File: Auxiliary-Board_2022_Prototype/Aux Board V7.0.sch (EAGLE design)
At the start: 56 parts, among them CON11 1X01, CON12 1X01, CON13 1X01, CON14 1X01, CON15 1X01, CON16 1X01, CON17 1X01, CON18 1X01, CON5 1X01, CON8 1X01, IC1 RS232-TTL_MAX232E

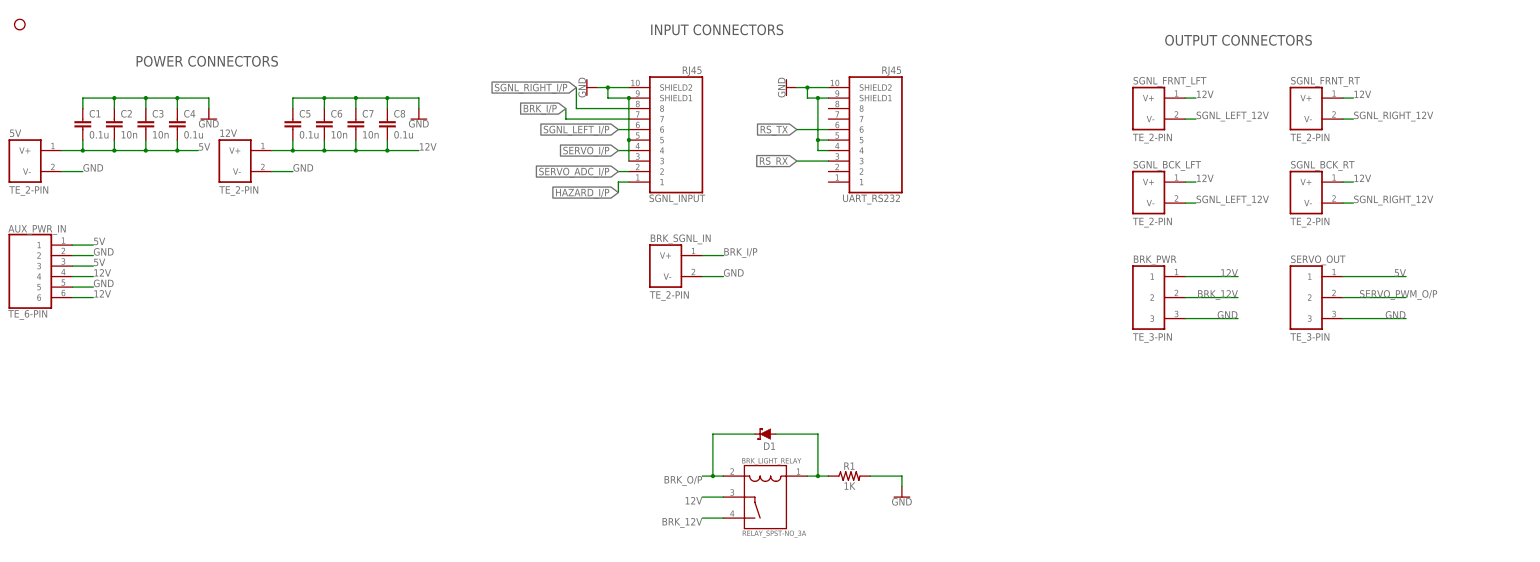
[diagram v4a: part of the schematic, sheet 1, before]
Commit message: feat: add EcoCar logo and version on board
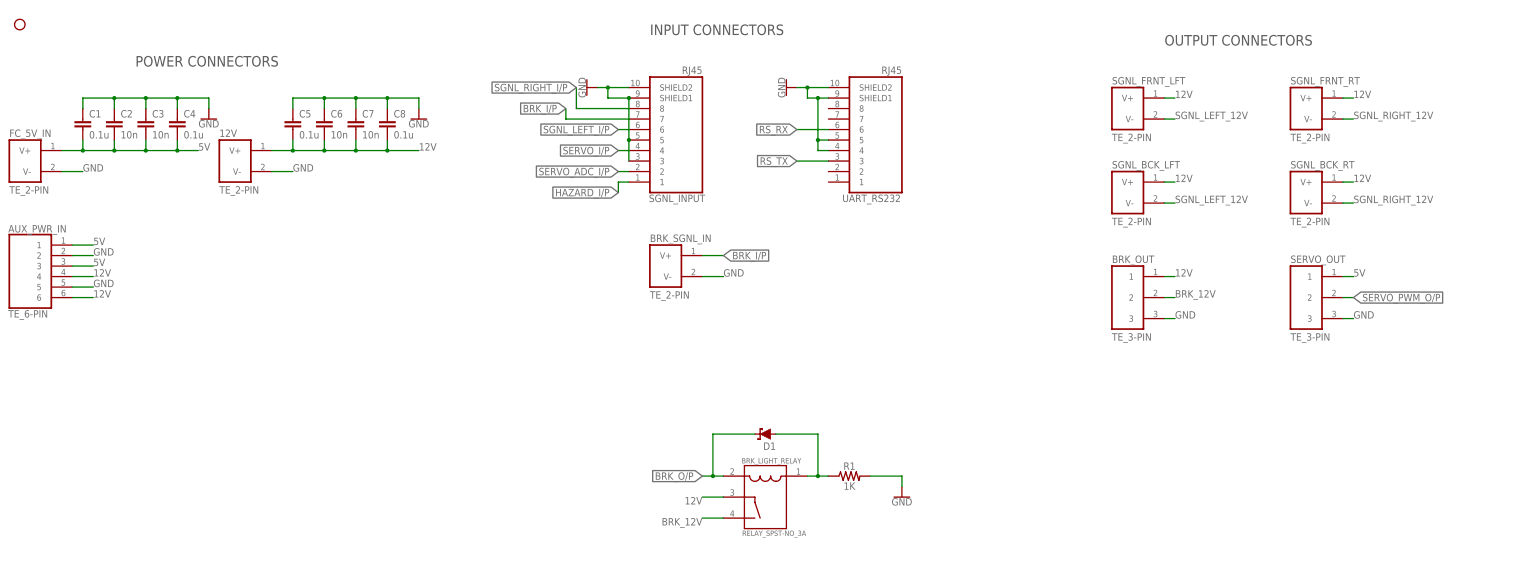
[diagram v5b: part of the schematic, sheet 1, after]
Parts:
- removed BRK_PWR: TE_3-PIN, EcoCar-Connectors:TE_3-PIN
- added BRK_OUT: TE_3-PIN, EcoCar-Connectors:TE_3-PIN
- renumbered 5V to FC_5V_IN
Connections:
- net 12V: now also BRK_OUT.1; no longer BRK_PWR.1
- net BRK_12V: now also BRK_OUT.2; no longer BRK_PWR.2
- net GND: now also BRK_OUT.3; no longer BRK_PWR.3
- net RS_RX: now also UART_RS232.6; no longer UART_RS232.3
- net RS_TX: now also UART_RS232.3; no longer UART_RS232.6
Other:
- moved on the sheet: SGNL_BCK_LFT, SGNL_FRNT_LFT
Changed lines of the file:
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@@
 <part name="CON17" library="EcoCar-Connectors-2.54mm" deviceset="1X01" device=""/>
 <part name="CON18" library="EcoCar-Connectors-2.54mm" deviceset="1X01" device=""/>
-<part name="5V" library="EcoCar-Connectors" deviceset="TE_2-PIN" device=""/>
+<part name="FC_5V_IN" library="EcoCar-Connectors" deviceset="TE_2-PIN" device=""/>
 <part name="12V" library="EcoCar-Connectors" deviceset="TE_2-PIN" device=""/>
-<part name="BRK_PWR" library="EcoCar-Connectors" deviceset="TE_3-PIN" device=""/>
+<part name="BRK_OUT" library="EcoCar-Connectors" deviceset="TE_3-PIN" device=""/>
 <part name="SERVO_OUT" library="EcoCar-Connectors" deviceset="TE_3-PIN" device=""/>
 <part name="C2" library="EcoCar-Passives" deviceset="CAPACITOR_0805" device="" value="10n"/>
@@
 <attribute name="NAME" x="274.32" y="-42.672" size="1.778" layer="95" font="vector"/>
 </instance>
-<instance part="5V" gate="G$1" x="-76.2" y="106.68" smashed="yes">
+<instance part="FC_5V_IN" gate="G$1" x="-76.2" y="106.68" smashed="yes">
 <attribute name="NAME" x="-76.2" y="117.602" size="1.778" layer="95" font="vector"/>
 <attribute name="VALUE" x="-76.2" y="103.886" size="1.778" layer="96" font="vector"/>
@@
 <attribute name="VALUE" x="-25.4" y="103.886" size="1.778" layer="96" font="vector"/>
 </instance>
-<instance part="BRK_PWR" gate="G$1" x="195.58" y="71.12" smashed="yes">
-<attribute name="NAME" x="195.58" y="87.122" size="1.778" layer="95" font="vector"/>
-<attribute name="VALUE" x="195.58" y="68.326" size="1.778" layer="96" font="vector"/>
+<instance part="BRK_OUT" gate="G$1" x="190.5" y="71.12" smashed="yes">
+<attribute name="NAME" x="190.5" y="87.122" size="1.778" layer="95" font="vector"/>
+<attribute name="VALUE" x="190.5" y="68.326" size="1.778" layer="96" font="vector"/>
 </instance>
 <instance part="SERVO_OUT" gate="G$1" x="233.68" y="71.12" smashed="yes">
@@
 <attribute name="VALUE" x="-76.454" y="73.914" size="1.778" layer="96" font="vector"/>
 </instance>
-<instance part="SGNL_FRNT_LFT" gate="G$1" x="195.58" y="119.38" smashed="yes">
-<attribute name="NAME" x="195.58" y="130.302" size="1.778" layer="95" font="vector"/>
-<attribute name="VALUE" x="195.58" y="116.586" size="1.778" layer="96" font="vector"/>
+<instance part="SGNL_FRNT_LFT" gate="G$1" x="190.5" y="119.38" smashed="yes">
+<attribute name="NAME" x="190.5" y="130.302" size="1.778" layer="95" font="vector"/>
+<attribute name="VALUE" x="190.5" y="116.586" size="1.778" layer="96" font="vector"/>
 </instance>
 <instance part="SGNL_FRNT_RT" gate="G$1" x="233.68" y="119.38" smashed="yes">
@@
 <attribute name="VALUE" x="233.68" y="116.586" size="1.778" layer="96" font="vector"/>
 </instance>
-<instance part="SGNL_BCK_LFT" gate="G$1" x="195.58" y="99.06" smashed="yes">
-<attribute name="NAME" x="195.58" y="109.982" size="1.778" layer="95" font="vector"/>
-<attribute name="VALUE" x="195.58" y="96.266" size="1.778" layer="96" font="vector"/>
+<instance part="SGNL_BCK_LFT" gate="G$1" x="190.5" y="99.06" smashed="yes">
+<attribute name="NAME" x="190.5" y="109.982" size="1.778" layer="95" font="vector"/>
+<attribute name="VALUE" x="190.5" y="96.266" size="1.778" layer="96" font="vector"/>
 </instance>
 <instance part="SGNL_BCK_RT" gate="G$1" x="233.68" y="99.06" smashed="yes">
@@
 </segment>
 <segment>
-<pinref part="5V" gate="G$1" pin="V-"/>
+<pinref part="FC_5V_IN" gate="G$1" pin="V-"/>
 <wire x1="-63.5" y1="109.22" x2="-58.42" y2="109.22" width="0.1524" layer="91"/>
 <label x="-58.42" y="109.22" size="1.778" layer="95"/>
@@
 </segment>
 <segment>
-<pinref part="BRK_PWR" gate="G$1" pin="3"/>
-<wire x1="208.28" y1="73.66" x2="220.98" y2="73.66" width="0.1524" layer="91"/>
-<label x="220.98" y="73.66" size="1.778" layer="95" align="bottom-right"/>
+<pinref part="BRK_OUT" gate="G$1" pin="3"/>
+<wire x1="203.2" y1="73.66" x2="205.74" y2="73.66" width="0.1524" layer="91"/>
+<label x="205.74" y="73.66" size="1.778" layer="95"/>
 </segment>
 <segment>
 <pinref part="SERVO_OUT" gate="G$1" pin="3"/>
-<wire x1="246.38" y1="73.66" x2="261.62" y2="73.66" width="0.1524" layer="91"/>
-<label x="261.62" y="73.66" size="1.778" layer="95" align="bottom-right"/>
+<wire x1="246.38" y1="73.66" x2="248.92" y2="73.66" width="0.1524" layer="91"/>
+<label x="248.92" y="73.66" size="1.778" layer="95"/>
 </segment>
 <segment>
@@
 </segment>
 <segment>
-<pinref part="BRK_PWR" gate="G$1" pin="1"/>
-<wire x1="208.28" y1="83.82" x2="220.98" y2="83.82" width="0.1524" layer="91"/>
-<label x="220.98" y="83.82" size="1.778" layer="95" align="bottom-right"/>
+<pinref part="BRK_OUT" gate="G$1" pin="1"/>
+<wire x1="203.2" y1="83.82" x2="205.74" y2="83.82" width="0.1524" layer="91"/>
+<label x="205.74" y="83.82" size="1.778" layer="95" rot="R180" align="top-right"/>
 </segment>
 <segment>
@@
 <segment>
 <pinref part="SGNL_FRNT_LFT" gate="G$1" pin="V+"/>
-<wire x1="208.28" y1="127" x2="210.82" y2="127" width="0.1524" layer="91"/>
-<label x="210.82" y="127" size="1.778" layer="95"/>
+<wire x1="203.2" y1="127" x2="205.74" y2="127" width="0.1524" layer="91"/>
+<label x="205.74" y="127" size="1.778" layer="95"/>
 </segment>
 <segment>
@@
 <segment>
 <pinref part="SGNL_BCK_LFT" gate="G$1" pin="V+"/>
-<wire x1="208.28" y1="106.68" x2="210.82" y2="106.68" width="0.1524" layer="91"/>
-<label x="210.82" y="106.68" size="1.778" layer="95"/>
+<wire x1="203.2" y1="106.68" x2="205.74" y2="106.68" width="0.1524" layer="91"/>
+<label x="205.74" y="106.68" size="1.778" layer="95"/>
 </segment>
 <segment>
@@
 <net name="5V" class="0">
 <segment>
-<pinref part="5V" gate="G$1" pin="V+"/>
+<pinref part="FC_5V_IN" gate="G$1" pin="V+"/>
 <label x="-30.48" y="114.3" size="1.778" layer="95"/>
 <wire x1="-63.5" y1="114.3" x2="-58.42" y2="114.3" width="0.1524" layer="91"/>
@@
 <segment>
 <pinref part="SERVO_OUT" gate="G$1" pin="1"/>
-<wire x1="246.38" y1="83.82" x2="261.62" y2="83.82" width="0.1524" layer="91"/>
-<label x="261.62" y="83.82" size="1.778" layer="95" align="bottom-right"/>
+<wire x1="246.38" y1="83.82" x2="248.92" y2="83.82" width="0.1524" layer="91"/>
+<label x="248.92" y="83.82" size="1.778" layer="95" rot="R180" align="top-right"/>
 </segment>
 <segment>
@@
 <pinref part="BRK_LIGHT_RELAY" gate="G$1" pin="2"/>
 <wire x1="96.52" y1="35.56" x2="93.98" y2="35.56" width="0.1524" layer="91"/>
-<label x="91.44" y="35.56" size="1.778" layer="95" rot="R180"/>
+<label x="91.44" y="35.56" size="1.778" layer="95" rot="R180" xref="yes"/>
 <wire x1="93.98" y1="35.56" x2="91.44" y2="35.56" width="0.1524" layer="91"/>
 <wire x1="93.98" y1="35.56" x2="93.98" y2="45.72" width="0.1524" layer="91"/>
@@
 <segment>
 <pinref part="BRK_SGNL_IN" gate="G$1" pin="V+"/>
-<label x="96.52" y="88.9" size="1.778" layer="95"/>
 <wire x1="91.44" y1="88.9" x2="96.52" y2="88.9" width="0.1524" layer="91"/>
+<label x="96.52" y="88.9" size="1.778" layer="95" xref="yes"/>
 </segment>
 <segment>
@@
 <segment>
 <pinref part="SERVO_OUT" gate="G$1" pin="2"/>
-<wire x1="246.38" y1="78.74" x2="261.62" y2="78.74" width="0.1524" layer="91"/>
-<label x="269.24" y="78.74" size="1.778" layer="95" align="bottom-right"/>
+<wire x1="246.38" y1="78.74" x2="248.92" y2="78.74" width="0.1524" layer="91"/>
+<label x="248.92" y="78.74" size="1.778" layer="95" xref="yes"/>
 </segment>
 </net>
@@
 <segment>
 <pinref part="SGNL_FRNT_LFT" gate="G$1" pin="V-"/>
-<wire x1="208.28" y1="121.92" x2="210.82" y2="121.92" width="0.1524" layer="91"/>
-<label x="210.82" y="121.92" size="1.778" layer="95"/>
+<wire x1="203.2" y1="121.92" x2="205.74" y2="121.92" width="0.1524" layer="91"/>
+<label x="205.74" y="121.92" size="1.778" layer="95"/>
 </segment>
 <segment>
 <pinref part="SGNL_BCK_LFT" gate="G$1" pin="V-"/>
-<wire x1="208.28" y1="101.6" x2="210.82" y2="101.6" width="0.1524" layer="91"/>
-<label x="210.82" y="101.6" size="1.778" layer="95"/>
+<wire x1="203.2" y1="101.6" x2="205.74" y2="101.6" width="0.1524" layer="91"/>
+<label x="205.74" y="101.6" size="1.778" layer="95"/>
 </segment>
 <segment>
@@
 <net name="BRK_12V" class="0">
 <segment>
-<pinref part="BRK_PWR" gate="G$1" pin="2"/>
-<wire x1="208.28" y1="78.74" x2="220.98" y2="78.74" width="0.1524" layer="91"/>
-<label x="220.98" y="78.74" size="1.778" layer="95" align="bottom-right"/>
+<pinref part="BRK_OUT" gate="G$1" pin="2"/>
+<wire x1="203.2" y1="78.74" x2="205.74" y2="78.74" width="0.1524" layer="91"/>
+<label x="205.74" y="78.74" size="1.778" layer="95"/>
 </segment>
 <segment>
@@
 </segment>
 <segment>
+<pinref part="UART_RS232" gate="G$1" pin="3"/>
+<wire x1="121.92" y1="111.76" x2="114.3" y2="111.76" width="0.1524" layer="91"/>
+<label x="114.3" y="111.76" size="1.778" layer="95" rot="R180" xref="yes"/>
+</segment>
+</net>
+<net name="RS_RX" class="0">
+<segment>
+<pinref part="IC1" gate="G$1" pin="ROUT1"/>
+<wire x1="-15.24" y1="-45.72" x2="-12.7" y2="-45.72" width="0.1524" layer="91"/>
+<label x="-12.7" y="-45.72" size="1.778" layer="95" xref="yes"/>
+</segment>
+<segment>
 <pinref part="UART_RS232" gate="G$1" pin="6"/>
 <wire x1="121.92" y1="119.38" x2="114.3" y2="119.38" width="0.1524" layer="91"/>
@@
 </segment>
 </net>
-<net name="RS_RX" class="0">
-<segment>
-<pinref part="IC1" gate="G$1" pin="ROUT1"/>
-<wire x1="-15.24" y1="-45.72" x2="-12.7" y2="-45.72" width="0.1524" layer="91"/>
-<label x="-12.7" y="-45.72" size="1.778" layer="95" xref="yes"/>
-</segment>
-<segment>
-<pinref part="UART_RS232" gate="G$1" pin="3"/>
-<wire x1="121.92" y1="111.76" x2="114.3" y2="111.76" width="0.1524" layer="91"/>
-<label x="114.3" y="111.76" size="1.778" layer="95" rot="R180" xref="yes"/>
-</segment>
-</net>

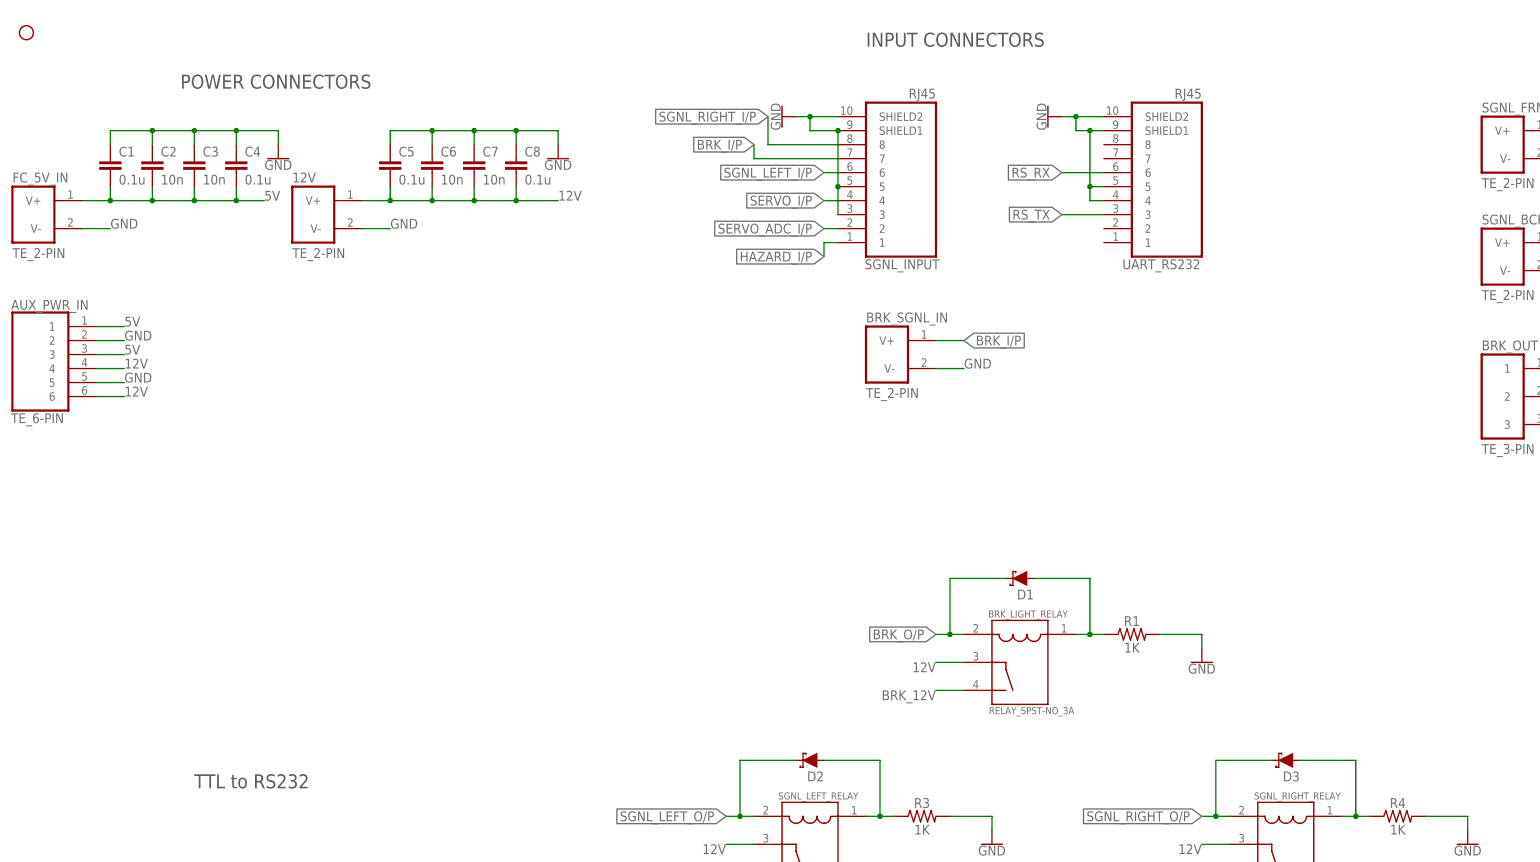
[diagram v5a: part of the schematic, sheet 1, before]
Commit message: feat: Add LEDs and fuses
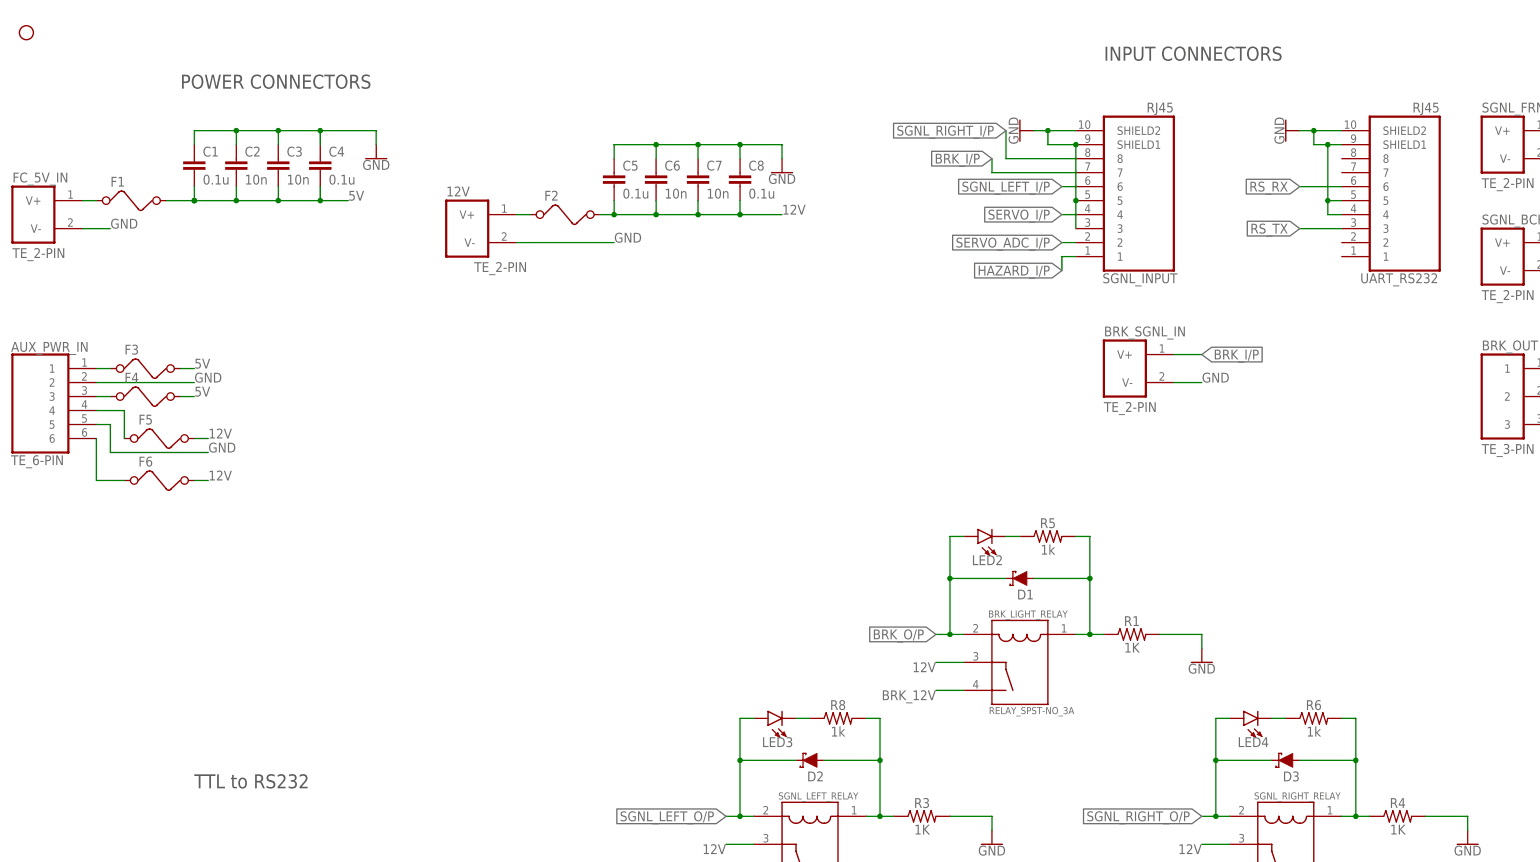
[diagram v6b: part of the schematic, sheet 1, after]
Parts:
- added F1, F2, F3, F4, F5, F6: (no value), EcoCar-Fuses-Protection:FUSE_1210
- added LED2, LED3, LED4: (no value), EcoCar-Discrete-Semiconductors:LED_0805
- added R5, R6, R8: 1k, EcoCar-Passives:RESISTOR_0805
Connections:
- new net N$30: LED2.C, R5.1
- new net N$31: LED4.C, R6.1
- new net N$32: LED3.C, R8.1
- new net N$33: F1.1, FC_5V_IN.V+
- new net N$35: 12V.V+, F2.1
- new net N$36: AUX_PWR_IN.1, F3.1
- new net N$37: AUX_PWR_IN.3, F4.1
- net 12V: now also F2.2, F5.1, F5.2, F6.1, F6.2; no longer 12V.V+
- net 5V: now also F1.2, F3.2, F4.2; no longer AUX_PWR_IN.1, AUX_PWR_IN.3, FC_5V_IN.V+
- net BRK_O/P: now also LED2.A
- net N$1: now also R5.2
- net N$13: now also R8.2
- net N$14: now also R6.2
- net SGNL_LEFT_O/P: now also LED3.A
- net SGNL_RIGHT_O/P: now also LED4.A
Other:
- moved on the sheet: 12V, AUX_PWR_IN, BRK_SGNL_IN, C1, C2, C3, C4, C5, C6, C7, C8, SGNL_INPUT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
